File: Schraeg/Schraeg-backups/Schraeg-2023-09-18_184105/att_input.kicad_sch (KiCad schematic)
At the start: 7 parts, among them U1 TL074

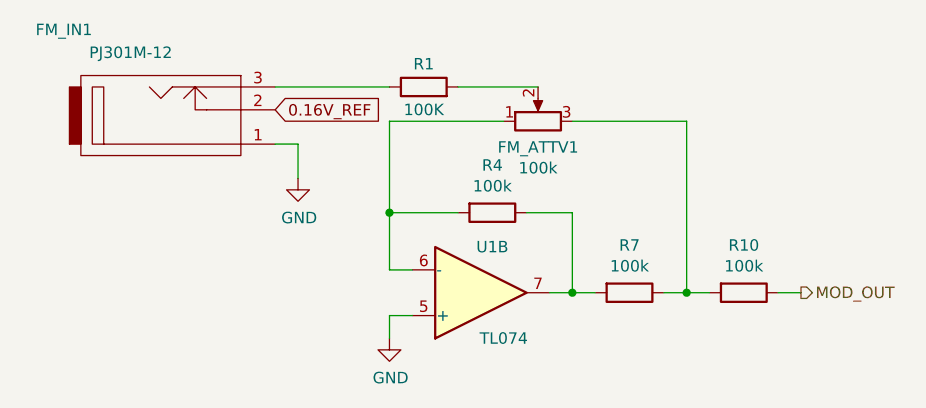
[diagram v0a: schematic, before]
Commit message: fixes filter schematic
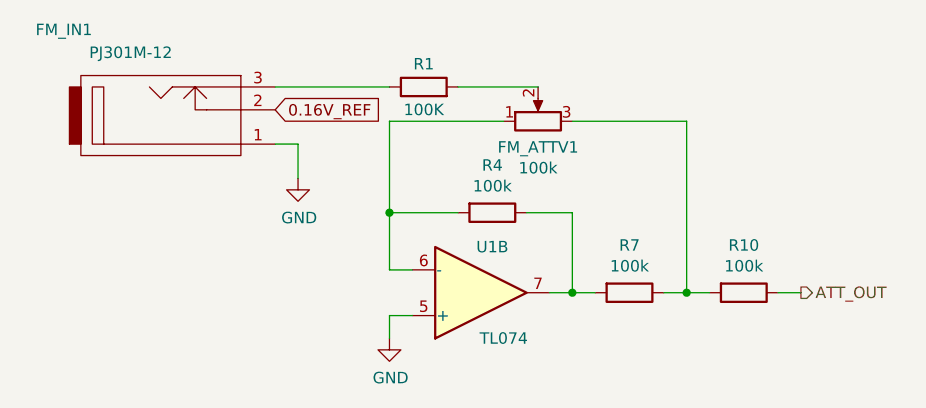
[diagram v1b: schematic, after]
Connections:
- net MOD_OUT renamed ATT_OUT
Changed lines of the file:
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@@
     )
   )
-  (hierarchical_label "MOD_OUT" (shape output) (at 182.88 93.98 0) (fields_autoplaced)
+  (hierarchical_label "ATT_OUT" (shape output) (at 182.88 93.98 0) (fields_autoplaced)
     (effects (font (size 1.27 1.27)) (justify left))
   )
@@
         )
         (path "/63ba224f-cd90-44e3-9d07-b2fc4e2de32b/5f66e1d5-9bed-43b2-93db-96b8aabdb30e"
-          (reference "MOD_IN") (unit 1)
+          (reference "FM_IN1") (unit 1)
         )
         (path "/63ba224f-cd90-44e3-9d07-b2fc4e2de32b/843512f8-0ffd-4dd1-8181-ca5b142ef288"
